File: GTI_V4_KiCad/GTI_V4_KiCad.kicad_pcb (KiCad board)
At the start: 4 copper layers, 155 x 75 mm, 141 parts, among them IC1 MASTERGAN2TR, IC2 MASTERGAN2TR, IC3 MAX253CSA+, IC4 AMC1306M25QDWVRQ1, IC5 AMC1306M25QDWVRQ1, IC6 AMC1306M25QDWVRQ1, IC7 MAX253CSA+, IC8 MAX253CSA+, IC9 AMC1306M25QDWVRQ1, J1 Screw_Terminal_01x03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

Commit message: Add files via upload
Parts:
- added C59: 1uF, Capacitor_SMD:C_0603_1608Metric, F.Cu at (172.9, 116.1)
- added C69: 100nF, Capacitor_SMD:C_0603_1608Metric, F.Cu at (106.0, 117.5)
- moved C75 29.5 mm to (77.1, 123.3), turned to 180 degrees
- moved C64 9.50 mm to (86.0, 109.5)
- moved C56 8.60 mm to (125.6, 113.0), turned to -90 degrees
- moved C38 3.15 mm to (163.4, 116.1), turned to -90 degrees
- moved C39 3.15 mm to (161.9, 116.1), turned to -90 degrees
- moved C45 1.20 mm to (171.4, 116.1), turned to -90 degrees
- moved C2 0.94 mm to (106.1, 105.1)
- moved Q2 0.40 mm to (115.2, 119.9)
- moved C19 0.10 mm to (63.1, 97.0)
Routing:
- net +3.3V: track 45.0 -> 36.7 mm, vias 15 -> 4
- net GNDD: track 81.2 -> 86.8 mm, vias 39 -> 58
- net /Relay: track 132.3 -> 134.7 mm
- net /Relay_Ctrl: track 16.2 -> 14.7 mm
- net PWM_B_H: track 48.1 -> 49.6 mm, vias 0 -> 2
- net D2_Sigma_Delta: track 82.0 -> 80.6 mm, vias 2 -> 0
- net CLK_SigmaDelta: track 116.6 -> 117.4 mm
- net /JTMS-SWDIO: track 5.53 -> 4.80 mm
- net PWM_A_H: track 44.5 -> 44.4 mm, vias 0 -> 2
- net D1_Sigma_Delta: vias 2 -> 0
- added copper zone on B.Cu, net +3.3V
- added copper zone on F.Cu, net +3.3V
- added copper zone on B.Cu, net +5V_1
- added copper zone on B.Cu, net +5V_2
- added copper zone on F.Cu, net +5V_2
- added copper zone on In2.Cu, net /Line_GND
- added copper zone on In2.Cu, net /Out_B
- added copper zone on B.Cu, net GNDD
- added copper zone on In2.Cu, net GNDD
- removed copper zone on In2.Cu, net +3.3V
- removed copper zone on In2.Cu, net +5V_1
- removed copper zone on In2.Cu, net +5V_2
- removed copper zone on In1.Cu, net /Line_GND
- removed copper zone on In1.Cu, net /Out_B

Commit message: 99% finished PCB
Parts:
- added C70: 100nF, Capacitor_SMD:C_0603_1608Metric, F.Cu at (107.2, 106.2)
- added C71: 10nF, Capacitor_SMD:C_0603_1608Metric, F.Cu at (182.6, 112.8)
- C73: moved to B.Cu
- moved C63 9.25 mm to (136.5, 116.3)
- moved C73 6.60 mm to (65.8, 117.9), turned to 180 degrees
- moved C61 6.31 mm to (128.5, 97.6)
- moved C55 4.50 mm to (124.8, 99.9)
- moved C56 3.23 mm to (124.4, 116.0)
- moved Q2 3.18 mm to (117.0, 117.2)
- moved J4 2.66 mm to (107.5, 118.0)
- moved C2 1.74 mm to (105.0, 103.8)
- moved C57 1.13 mm to (122.9, 116.0), turned to -90 degrees
- moved C10 1.00 mm to (98.2, 101.5)
- moved C69 0.92 mm to (105.3, 118.1), turned to -90 degrees
- moved PS3 0.91 mm to (127.4, 100.5), turned to 90 degrees
- moved C1 0.75 mm to (92.8, 114.8)
- moved JP1 0.50 mm to (108.2, 109.5), turned to 90 degrees
- moved C8 0.44 mm to (73.9, 59.3)
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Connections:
- net /JTCK-SWCLK renamed /SWCLK
- J4 pad 1: /JTMS-SWDIO -> +3.3V
- J4 pad 3: /JTDI -> GNDD
- J4 pad 4: /JTDO-TRACESWO -> /SWDIO
- J4 pad 5: /NJTRST -> /NRST
- J4 pad 6: GNDD -> /SWO
- U1 pad 46: /JTMS-SWDIO -> /SWDIO
- U1 pad 50: /JTDI -> unconnected-(U1-Pad50)
- U1 pad 55: /JTDO-TRACESWO -> /SWO
- U1 pad 56: /NJTRST -> unconnected-(U1-Pad56)
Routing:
- net +3.3V: track 36.7 -> 204.8 mm, vias 4 -> 17
- net /NRST: track 5.89 -> 32.5 mm, vias 0 -> 1
- net VBUS: track 2.67 -> 19.1 mm
- net +5V: track 132.2 -> 147.0 mm
- net VCC: track 203.4 -> 191.1 mm
- net /SWDIO: track 0.00 -> 12.1 mm
- net /NJTRST: track 11.6 -> 0.00 mm, vias 1 -> 0
- net /SWO: track 0.00 -> 10.4 mm
- net /JTDO-TRACESWO: track 10.0 -> 0.00 mm, vias 1 -> 0
- net D4_Sigma_Delta: track 20.7 -> 29.3 mm, vias 2 -> 0
- net /JTDI: track 7.81 -> 0.00 mm, vias 1 -> 0
- net +5V_1: track 13.2 -> 19.9 mm
- net /Relay: track 134.7 -> 128.7 mm
- net /JTMS-SWDIO: track 4.80 -> 0.00 mm
- net /Relay_Ctrl: track 14.7 -> 19.2 mm
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- added copper zone on B.Cu, net +5VD
- added copper zone on F.Cu, net +5V_1
- added copper zone on In1.Cu, net /Line_GND
- added copper zone on In1.Cu, net /Out_B
- added copper zone on In2.Cu, net GND
- added copper zone on F.Cu, net GNDD
- removed copper zone on F.Cu, net +3.3V
- removed copper zone on In2.Cu, net +5VD
- removed copper zone on B.Cu, net +5V_1
- removed copper zone on B.Cu, net +5V_2
- removed copper zone on F.Cu, net +5V_2
- removed copper zone on In2.Cu, net /Line_GND
- removed copper zone on In2.Cu, net /Out_B
- removed copper zone on B.Cu, net GNDD
- removed copper zone on In2.Cu, net VBUS

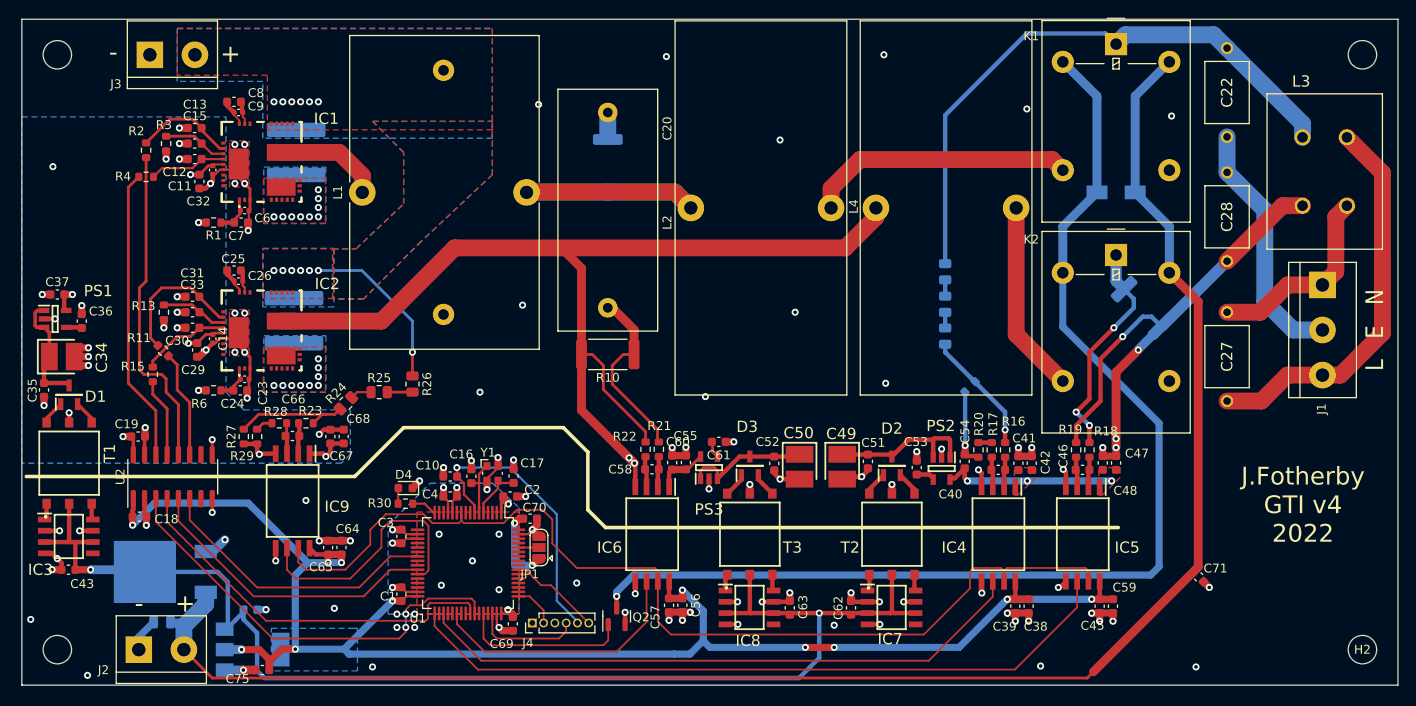
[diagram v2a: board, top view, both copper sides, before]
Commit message: Completed PCB - sent for fabrication
Sent to PCBWay for fabrication
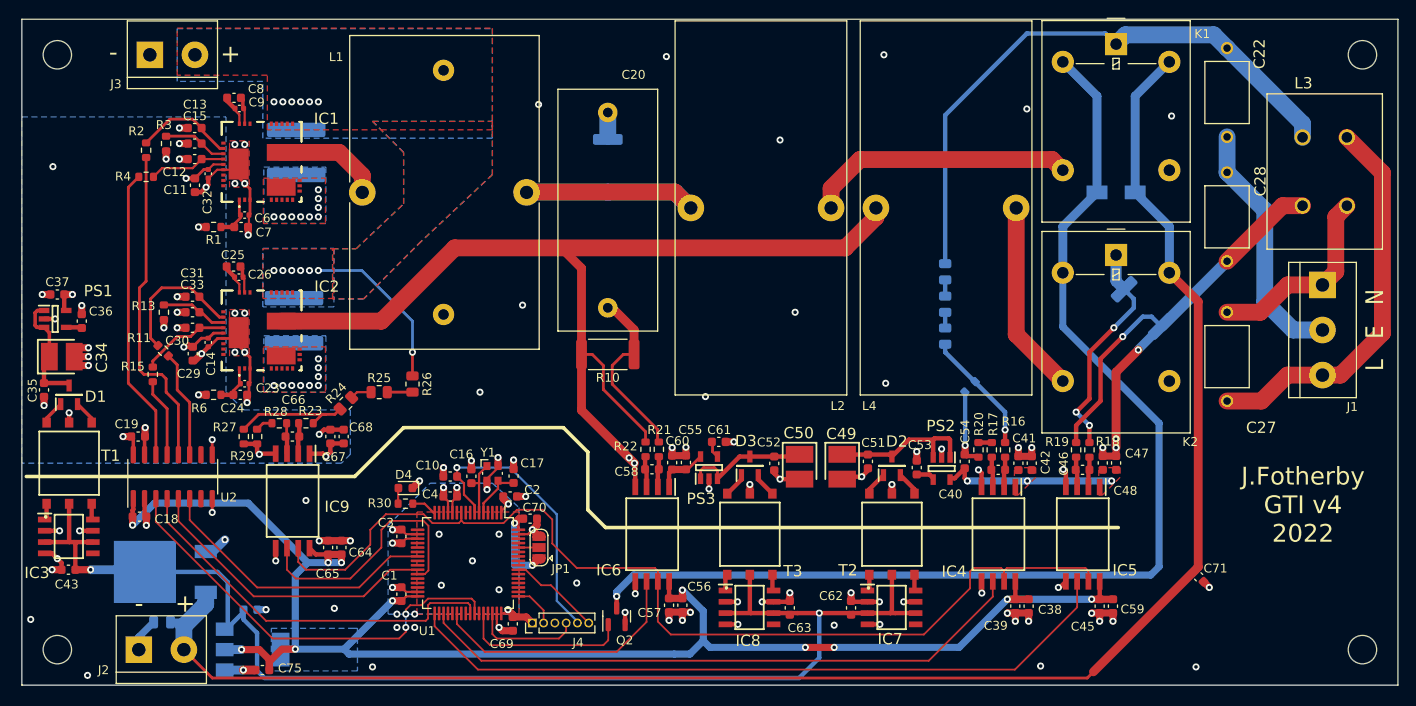
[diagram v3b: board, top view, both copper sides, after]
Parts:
- moved C14 0.65 mm to (71.0, 86.4)
- moved C29 0.65 mm to (69.2, 87.7)
- moved C32 0.65 mm to (71.0, 67.4)
- moved C11 0.65 mm to (69.5, 68.7)
- moved C23 0.50 mm to (75.1, 91.0)
- moved C24 0.50 mm to (74.6, 92.3)
- moved C6 0.50 mm to (75.1, 72.0)
- moved C7 0.50 mm to (74.7, 73.4)
- moved R1 0.50 mm to (71.6, 73.4)
- moved R6 0.50 mm to (71.6, 92.3)
- moved C9 0.46 mm to (74.5, 60.0)
- moved C25 0.45 mm to (73.8, 77.8)
- moved C26 0.45 mm to (74.5, 79.0)
- moved C8 0.45 mm to (73.9, 58.9)
- moved C66 0.06 mm to (80.5, 97.0)
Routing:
- net GND: track 56.8 -> 59.2 mm
- net +5VD: track 23.3 -> 24.6 mm
- net +3.3V: track 204.8 -> 206.0 mm
- net Net-(C40-Pad2): track 3.74 -> 3.13 mm
- net Net-(C6-Pad1): track 4.41 -> 4.91 mm
- net Net-(C23-Pad1): track 4.25 -> 4.75 mm
